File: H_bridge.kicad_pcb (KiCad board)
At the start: 2 copper layers, 32 x 21 mm, 23 parts, among them J1 Conn_01x04_Socket, J2 Conn_01x04_Socket, J3 Conn_01x04_Socket, J4 Conn_01x04_Socket, J5 Conn_01x04_Socket, J6 Conn_01x04_Socket, J7 Conn_01x04_Socket, U1 VNH7040AYTR

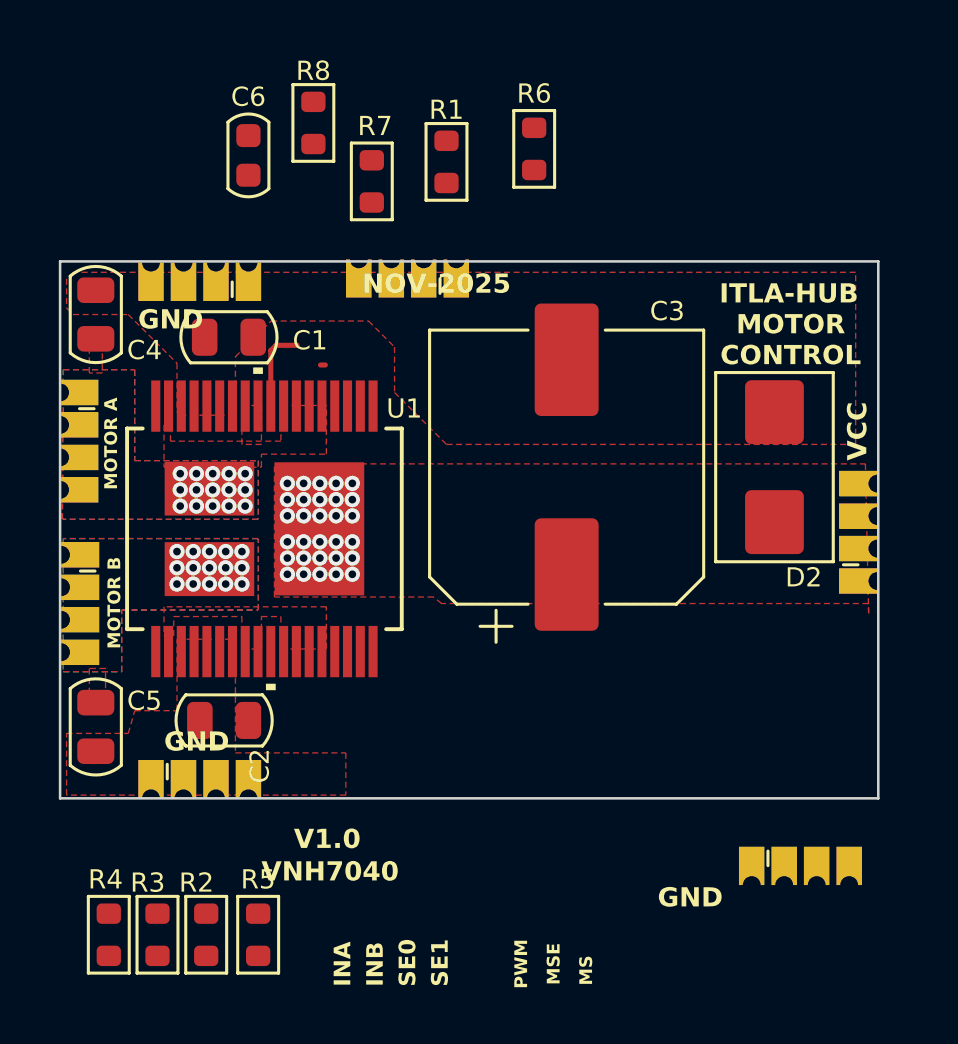
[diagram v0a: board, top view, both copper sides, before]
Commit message: Primera version preliminar Conexiones y cobre completado Falta verificar las reglas y el BOM
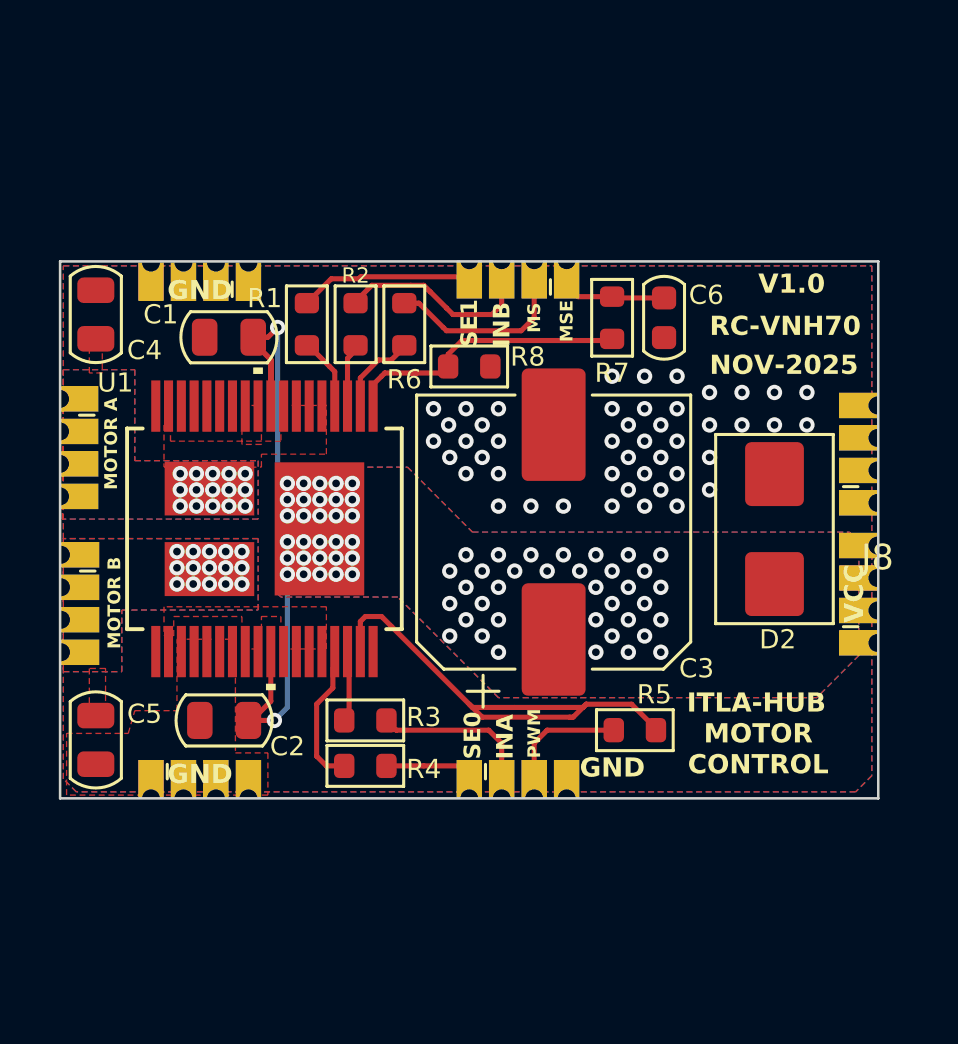
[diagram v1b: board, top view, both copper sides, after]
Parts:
- added J8: Conn_01x04_Socket, Connector_PinSocket_1.27mm:PinSocket_1x04_P1.27mm_Castellated, F.Cu at (144.2, 74.2)
- moved R2 24.6 mm to (123.8, 67.2), turned to -90 degrees
- moved C6 17.5 mm to (135.9, 67.0)
- moved R5 16.8 mm to (134.7, 83.1), turned to 0 degrees
- moved R4 12.0 mm to (124.2, 84.5), turned to 180 degrees
- moved R3 11.7 mm to (124.2, 82.7), turned to 180 degrees
- moved J2 11.6 mm to (128.3, 85.8)
- moved R8 11.3 mm to (128.3, 68.9), turned to 180 degrees
- moved R7 10.8 mm to (133.8, 67.0), turned to -90 degrees
- moved R6 8.53 mm to (125.7, 67.2), turned to -90 degrees
- moved R1 8.38 mm to (121.9, 67.2), turned to -90 degrees
- moved J1 4.32 mm to (132.1, 64.7)
- moved C3 2.59 mm to (131.6, 75.3)
- moved D2 2.42 mm to (140.2, 75.2)
- moved J3 2.42 mm to (144.2, 79.7)
- moved C5 0.51 mm to (113.6, 83.5)
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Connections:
- J2 pad 4: unconnected-(J2-Pin_4-Pad4) -> GND
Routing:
- net Net-(U1-PWM): track 0.00 -> 19.6 mm
- net VCC: track 3.30 -> 22.6 mm, vias 30 -> 68
- net Net-(U1-MultiSense): track 0.00 -> 11.3 mm
- net /in_b: track 0.00 -> 7.19 mm
- net /m_sense_en: track 0.00 -> 7.13 mm
- net /sel1: track 0.00 -> 6.65 mm
- net /in_a: track 0.00 -> 6.02 mm
- net Net-(U1-Sel0): track 0.00 -> 4.93 mm
- net /pwm: track 0.00 -> 4.34 mm
- net /m_sense: track 0.00 -> 4.03 mm
- net Net-(U1-MultiSense_EN): track 0.00 -> 3.32 mm
- net /sel0: track 0.00 -> 2.98 mm
- net Net-(U1-Sel1): track 0.19 -> 2.84 mm
- net Net-(U1-Input_A): track 0.00 -> 2.62 mm
- net Net-(U1-Input_B): track 0.00 -> 2.49 mm
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- added copper zone on B.Cu, net GND
- added copper zone on B.Cu, net VCC
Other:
- board text added: "RC-VNH70"
- board text removed: "VNH7040"

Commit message: Actualizaciones de diseno genetrales.
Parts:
- moved J1 0.09 mm to (132.1, 64.8)
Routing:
- net Net-(U1-PWM): track 19.6 -> 15.3 mm
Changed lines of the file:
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@@
 	)
 	(footprint "Connector_PinSocket_1.27mm:PinSocket_1x04_P1.27mm_Castellated"
+		(locked yes)
 		(layer "F.Cu")
 		(at 119.616 64.795 -90)
@@
 		)
 		(embedded_fonts no)
-		(model "${MG_3DMODEL_DIR}/POWERSSO-36TP_STM.step"
+		(model "${KICAD_3RD_PARTY}/EasyEDA.3dshapes/POWERSSO-36_L10.3-W7.5-H2.3-P0.50-LS10.3-BL-EP_VNH5050ATR-E.step"
 			(offset
-				(xyz 0 0 0)
+				(xyz 0 0 1.2)
 			)
 			(scale
@@
 			)
 			(rotate
-				(xyz 0 0 0)
+				(xyz -0 -0 -90)
 			)
 		)
@@
 	(footprint "Connector_PinSocket_1.27mm:PinSocket_1x04_P1.27mm_Castellated"
 		(layer "F.Cu")
-		(at 132.062 64.705 -90)
+		(at 132.062 64.795 -90)
 		(descr "Through hole straight socket strip, 1x04, 1.27mm pitch, single row (from Kicad 4.0.7), script generated")
 		(tags "Through hole socket strip THT 1x04 1.27mm single row")
@@
 	)
 	(gr_text "SE0"
-		(at 128.76 84.226 90)
+		(at 131.3 84.226 90)
 		(layer "F.SilkS")
 		(effects
@@
 	)
 	(gr_text "PWM"
-		(at 130.792 83.21 90)
+		(at 128.125 83.21 90)
 		(layer "F.SilkS")
 		(effects
@@
 	)
 	(segment
-		(start 130.03 82.194)
-		(end 132.697 82.194)
-		(width 0.2)
-		(layer "F.Cu")
-		(net 9)
-	)
-	(segment
 		(start 134.602 82.067)
 		(end 135.364 82.829)
@@
 	)
 	(segment
-		(start 128.379 82.194)
-		(end 130.03 82.194)
-		(width 0.2)
-		(layer "F.Cu")
-		(net 9)
-	)
-	(segment
 		(start 124.823 78.638)
 		(end 125.204 79.019)
@@
 	)
 	(segment
-		(start 132.697 82.194)
-		(end 132.824 82.067)
-		(width 0.2)
-		(layer "F.Cu")
-		(net 9)
-	)
-	(segment
-		(start 132.824 82.067)
-		(end 134.602 82.067)
+		(start 135.364 82.829)
+		(end 135.364 82.956)
 		(width 0.2)
 		(layer "F.Cu")
@@
 	)
 	(segment
-		(start 135.364 82.829)
-		(end 135.364 82.956)
+		(start 132.697 82.194)
+		(end 132.824 82.067)
 		(width 0.2)
 		(layer "F.Cu")
@@
 		(width 0.2)
 		(layer "F.Cu")
+		(net 9)
+	)
+	(segment
+		(start 132.824 82.067)
+		(end 134.602 82.067)
+		(width 0.2)
+		(layer "F.Cu")

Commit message: Version 1 enviada a fabricacion
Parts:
- removed C1, C2: C_0805, Capacitor_SMD_AKL:C_0805_2012Metric
- C4, C5: value C_0805 -> 100NF
- R1: value 1k -> 1K
- R2, R3, R4, R5, R6: value R_0603 -> 1K
- R7: value 10k -> 10K
- R8: value 1k -> 1.5K
- moved R4 11.5 mm to (135.6, 83.7), turned to 90 degrees
- moved R5 10.6 mm to (124.3, 84.5), turned to 180 degrees
- moved R1 0.74 mm to (121.9, 66.5)
- moved R2 0.71 mm to (123.8, 66.5)
- moved R3 0.14 mm to (124.3, 82.6)
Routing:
- net Net-(U1-Sel0): track 4.93 -> 15.8 mm
- net Net-(U1-PWM): track 15.3 -> 4.95 mm
- net VCC: track 22.6 -> 12.9 mm, vias 68 -> 0
- net /sel0: track 2.98 -> 7.80 mm
- net Net-(U1-Sel1): track 2.84 -> 4.03 mm
- net /in_a: track 6.02 -> 6.94 mm
- net /pwm: track 4.34 -> 5.22 mm
- net Net-(U1-Input_B): track 2.49 -> 3.22 mm
- net GND: vias 46 -> 36
- net /motor_b: vias 15 -> 0
- net /motor_a: vias 15 -> 0
- removed copper zone on B.Cu, net /motor_a
- removed copper zone on B.Cu, net /motor_b
- removed copper zone on B.Cu, net VCC
